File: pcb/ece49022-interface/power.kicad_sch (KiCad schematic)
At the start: 16 parts, among them U4 NCP1117-3.3_SOT223, U5 TPS54202DDCT

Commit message: update for pcb
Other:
- moved on the sheet: C21, C23, C24, C26, C27, C29, C31, C33, L2, R12, R13, R16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

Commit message: Initial PCB
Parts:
- removed C24, C27: 10u, Capacitor_SMD:C_0805_2012Metric, symbol Device:C
- removed U4: NCP1117-3.3_SOT223, Package_TO_SOT_SMD:SOT-223-3_TabPin2, symbol Regulator_Linear:NCP1117-3.3_SOT223

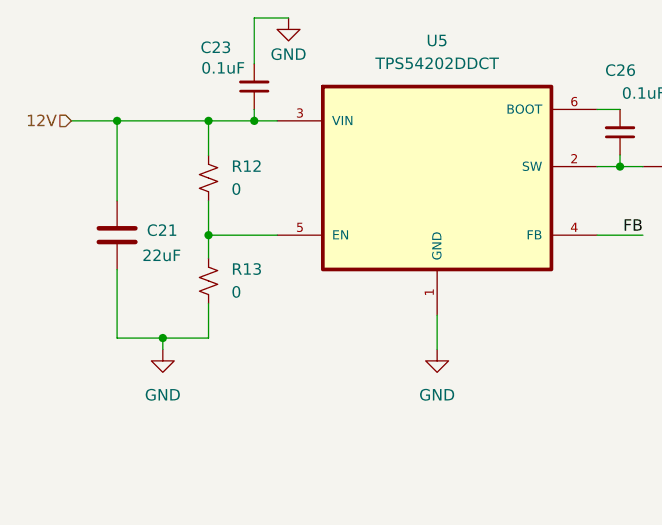
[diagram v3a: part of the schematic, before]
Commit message: update power resistors, wiring
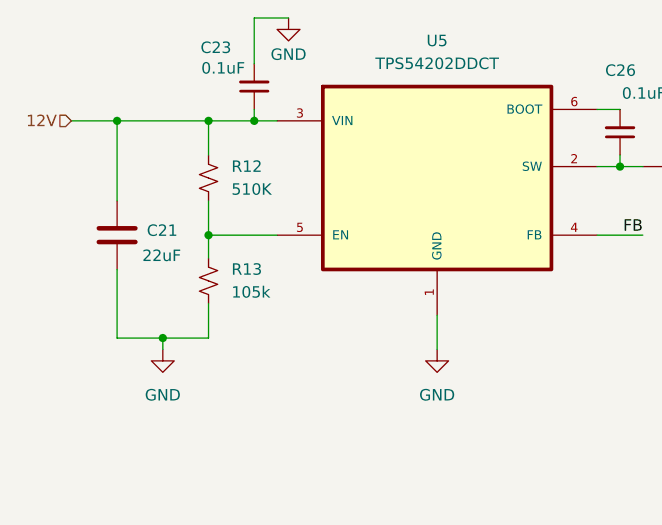
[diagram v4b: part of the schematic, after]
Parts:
- R12: value 0 -> 510K
- R13: value 0 -> 105k

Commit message: update
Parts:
- removed C21: 22uF, Capacitor_SMD:C_0805_2012Metric_Pad1.18x1.45mm_HandSolder, symbol Device:C
- removed C23, C26: 0.1uF, Capacitor_SMD:C_0402_1005Metric, symbol Device:C_Small
- removed C29, C31: 22uF,25V, Capacitor_SMD:C_0805_2012Metric_Pad1.18x1.45mm_HandSolder, symbol Device:C
- removed C33: 75pF, Capacitor_SMD:C_0402_1005Metric, symbol Device:C_Small
- removed R16: 49.9, 1%, Capacitor_SMD:C_0402_1005Metric, symbol Device:R_Small_US
- removed R17: 100k, 1%, Capacitor_SMD:C_0402_1005Metric, symbol Device:R_Small_US
- removed R18: 13.3k, 1%, Capacitor_SMD:C_0402_1005Metric, symbol Device:R_Small_US
- removed U5: TPS54202DDCT, 49022_Footprints:TPS54202, symbol ECE49022_Symbols:TPS54202DDCT
- added C10, C11: 22uF,25V, Capacitor_SMD:C_0805_2012Metric_Pad1.18x1.45mm_HandSolder, symbol Device:C
- added C12: 75pF, Capacitor_SMD:C_0402_1005Metric, symbol Device:C_Small
- added C7: 22uF, Capacitor_SMD:C_1206_3216Metric, symbol Device:C
- added C8, C9: 0.1uF, Capacitor_SMD:C_0402_1005Metric, symbol Device:C_Small
- added R10: 105k, Capacitor_SMD:C_0402_1005Metric, symbol Device:R_Small_US
- added R14: 13.3k, 1%, Capacitor_SMD:C_0402_1005Metric, symbol Device:R_Small_US
- added R9: 510K, Capacitor_SMD:C_0402_1005Metric, symbol Device:R_Small_US
- added U2: TPS54202DDCT, 49022_Footprints:TPS54202, symbol ECE49022_Symbols:TPS54202DDCT
- R12: value 510K -> 49.9, 1%
- R13: value 105k -> 100k, 1%
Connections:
- net 12V: now also C7.1, C8.1, R9.1, U2.3 (VIN); no longer R12.1
- net 5V: now also R12.1, C10.1, C11.1
- net FB: now also R13.2, C12.2, R14.1, U2.4 (FB)
- net GND: now also C10.2, C11.2, C7.2, C8.2, R10.2, R14.2, U2.1 (GND); no longer R13.2
- net at R12.2, R13.1: now also C12.1
- net at L2.1: now also C9.1, U2.2 (SW)
- new net: C9.2, U2.6 (BOOT)
- new net: R10.1, R9.2, U2.5 (EN)
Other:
- moved on the sheet: L2
